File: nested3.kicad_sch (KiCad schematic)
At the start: 5 parts, among them U5 INA219AIDR

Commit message: made changes to USB circuit
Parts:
- C7: value CL05B104KO5NNNC -> 100n
- R5: value RL1206FR-070R05L -> 0.05
- R6, R7: value 1206W4F1002T5E -> 10k
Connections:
- net Battery: now reaches R5.1, U5.8 (VIN+)
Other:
- note added: "Vreg cct"
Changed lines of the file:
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@@
 		(comment 4 "Phila Haanyama, Hannah Owen")
 	)
+	(text "Vreg cct"
+		(exclude_from_sim no)
+		(at 104.648 120.142 0)
+		(effects
+			(font
+				(size 1.27 1.27)
+			)
+		)
+	)
+	(junction
+		(at 106.68 114.3)
+		(diameter 0)
+		(color 0 0 0 0)
+	)
+	(junction
+		(at 72.39 101.6)
+		(diameter 0)
+		(color 0 0 0 0)
+	)
 	(wire
 		(pts
@@
 	(wire
 		(pts
+			(xy 62.23 101.6) (xy 72.39 101.6)
+		)
+		(stroke
+			(width 0)
+			(type default)
+		)
+	)
+	(wire
+		(pts
 			(xy 104.14 88.9) (xy 107.95 88.9)
 		)
@@
 		(pts
 			(xy 143.51 114.3) (xy 147.32 114.3)
+		)
+		(stroke
+			(width 0)
+			(type default)
+		)
+	)
+	(wire
+		(pts
+			(xy 106.68 114.3) (xy 106.68 121.92)
 		)
 		(stroke
@@
 				)
 				(justify left)
+				(hide yes)
+			)
+		)
+	)
+	(global_label "Battery"
+		(shape input)
+		(at 62.23 101.6 180)
+		(fields_autoplaced yes)
+		(effects
+			(font
+				(size 1.27 1.27)
+			)
+			(justify right)
+		)
+		(property "Intersheetrefs" "${INTERSHEET_REFS}"
+			(at 52.532 101.6 0)
+			(effects
+				(font
+					(size 1.27 1.27)
+				)
+				(justify right)
 				(hide yes)
 			)
@@
 			)
 		)
-		(property "Value" "1206W4F1002T5E"
+		(property "Value" "10k"
 			(at 49.53 92.71 0)
 			(effects
@@
 			)
 		)
-		(property "Value" "RL1206FR-070R05L"
+		(property "Value" "0.05"
 			(at 85.09 110.49 0)
 			(effects
@@
 			)
 		)
-		(property "Value" "CL05B104KO5NNNC"
+		(property "Value" "100n"
 			(at 166.37 86.3599 90)
 			(effects
@@
 			)
 		)
-		(property "Value" "1206W4F1002T5E"
+		(property "Value" "10k"
 			(at 74.93 142.24 0)
 			(effects

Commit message: footprints added and usb cct finished
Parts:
- C7: footprint CL05B104KO5NNNC:CAPC1005X55N -> Capacitor_SMD:C_0402_1005Metric_Pad0.74x0.62mm_HandSolder
- R5: footprint RL1206FR-070R05L:RESC3116X65N -> Resistor_SMD:R_1206_3216Metric_Pad1.30x1.75mm_HandSolder
- R6, R7: footprint 1206W4F1002T5E:RESC3115X65N -> Resistor_SMD:R_1206_3216Metric_Pad1.30x1.75mm_HandSolder
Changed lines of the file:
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@@
 			)
 		)
-		(property "Footprint" "1206W4F1002T5E:RESC3115X65N"
+		(property "Footprint" "Resistor_SMD:R_1206_3216Metric_Pad1.30x1.75mm_HandSolder"
 			(at 49.53 96.52 0)
 			(effects
@@
 			)
 		)
-		(property "Footprint" "RL1206FR-070R05L:RESC3116X65N"
+		(property "Footprint" "Resistor_SMD:R_1206_3216Metric_Pad1.30x1.75mm_HandSolder"
 			(at 85.09 114.3 0)
 			(effects
@@
 			)
 		)
-		(property "Footprint" "CL05B104KO5NNNC:CAPC1005X55N"
+		(property "Footprint" "Capacitor_SMD:C_0402_1005Metric_Pad0.74x0.62mm_HandSolder"
 			(at 162.56 83.82 0)
 			(effects
@@
 			)
 		)
-		(property "Footprint" "1206W4F1002T5E:RESC3115X65N"
+		(property "Footprint" "Resistor_SMD:R_1206_3216Metric_Pad1.30x1.75mm_HandSolder"
 			(at 74.93 146.05 0)
 			(effects

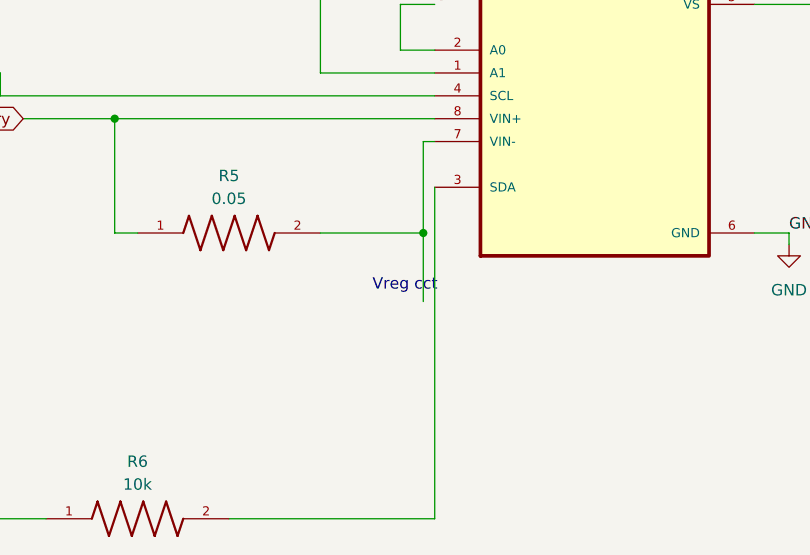
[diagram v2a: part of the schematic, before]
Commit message: added LCSC numbers and finsihed footprints
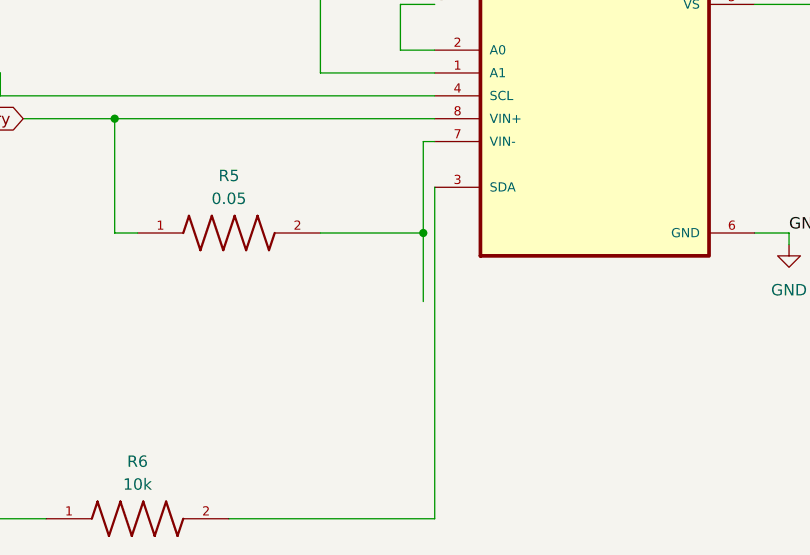
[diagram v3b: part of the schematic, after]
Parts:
- C7: LCSC (none) -> C1525
- R5: LCSC (none) -> C375525
- R6, R7: LCSC (none) -> C17902
- U5: footprint INA219AIDR:SOIC127P599X175-8N -> Package_SO:SOIC-8_3.9x4.9mm_P1.27mm; LCSC (none) -> C138706
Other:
- note removed: "Vreg cct"
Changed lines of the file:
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@@
 		(comment 4 "Phila Haanyama, Hannah Owen")
-	)
-	(text "Vreg cct"
-		(exclude_from_sim no)
-		(at 104.648 120.142 0)
-		(effects
-			(font
-				(size 1.27 1.27)
-			)
-		)
 	)
 	(junction
@@
 			)
 		)
+		(property "LCSC" "C17902"
+			(at 49.53 96.52 0)
+			(effects
+				(font
+					(size 1.27 1.27)
+				)
+				(hide yes)
+			)
+		)
 		(pin "1"
 		)
@@
 			)
 		)
+		(property "LCSC" "C375525"
+			(at 85.09 114.3 0)
+			(effects
+				(font
+					(size 1.27 1.27)
+				)
+				(hide yes)
+			)
+		)
 		(pin "2"
 		)
@@
 			)
 		)
+		(property "LCSC" "C1525"
+			(at 162.56 83.82 90)
+			(effects
+				(font
+					(size 1.27 1.27)
+				)
+				(hide yes)
+			)
+		)
 		(pin "1"
 		)
@@
 			)
 		)
-		(property "Footprint" "INA219AIDR:SOIC127P599X175-8N"
+		(property "Footprint" "Package_SO:SOIC-8_3.9x4.9mm_P1.27mm"
 			(at 125.73 101.6 0)
 			(effects
@@
 				)
 				(justify bottom)
+				(hide yes)
+			)
+		)
+		(property "LCSC" "C138706"
+			(at 125.73 101.6 0)
+			(effects
+				(font
+					(size 1.27 1.27)
+				)
 				(hide yes)
 			)
@@
 				(hide yes)
 			)
+		)
+		(property "LCSC" "C17902"
+			(at 74.93 146.05 0)
+			(effects
+				(font
+					(size 1.27 1.27)
+				)
+				(hide yes)
+			)

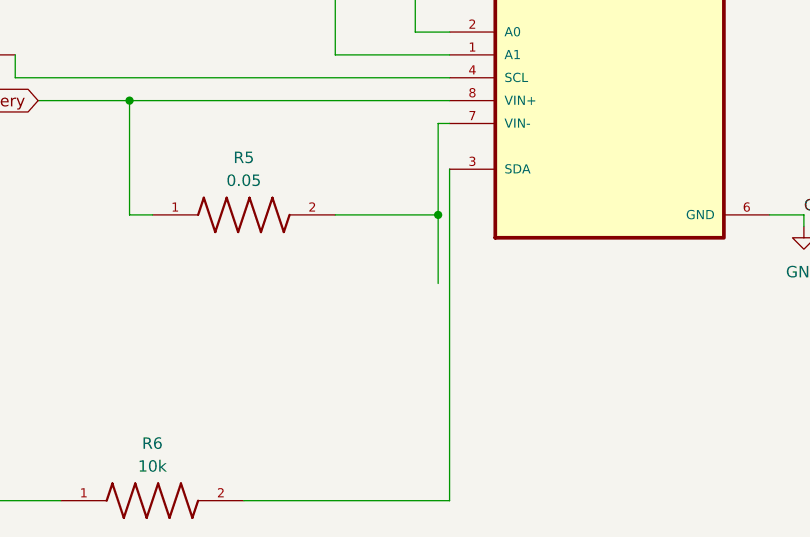
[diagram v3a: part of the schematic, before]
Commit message: Removed old backups and updated KiCad files
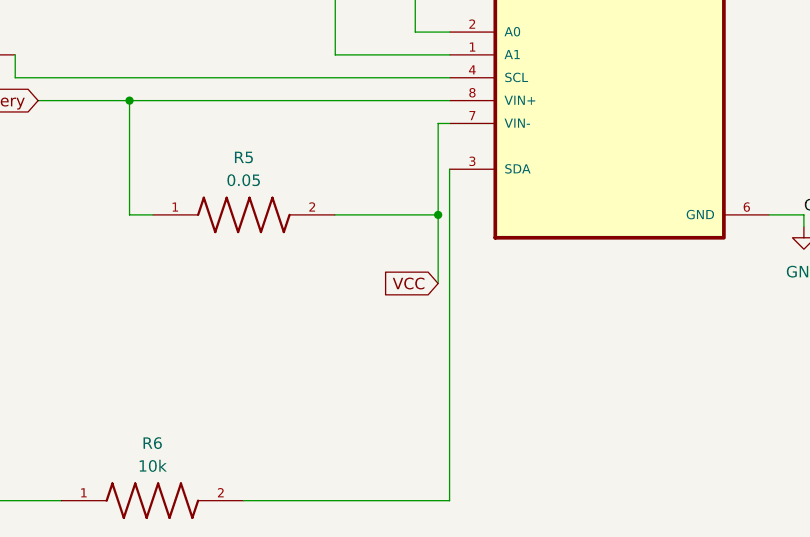
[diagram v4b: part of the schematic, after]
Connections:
- net VCC: now reaches R5.2, U5.7 (VIN-)
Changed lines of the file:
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@@
+		)
+	)
+	(global_label "VCC"
+		(shape input)
+		(at 106.68 121.92 180)
+		(fields_autoplaced yes)
+		(effects
+			(font
+				(size 1.27 1.27)
+			)
+			(justify right)
+		)
+		(property "Intersheetrefs" "${INTERSHEET_REFS}"
+			(at 100.0662 121.92 0)
+			(effects
+				(font
+					(size 1.27 1.27)
+				)
+				(justify right)
+				(hide yes)
+			)
 		)
 	)

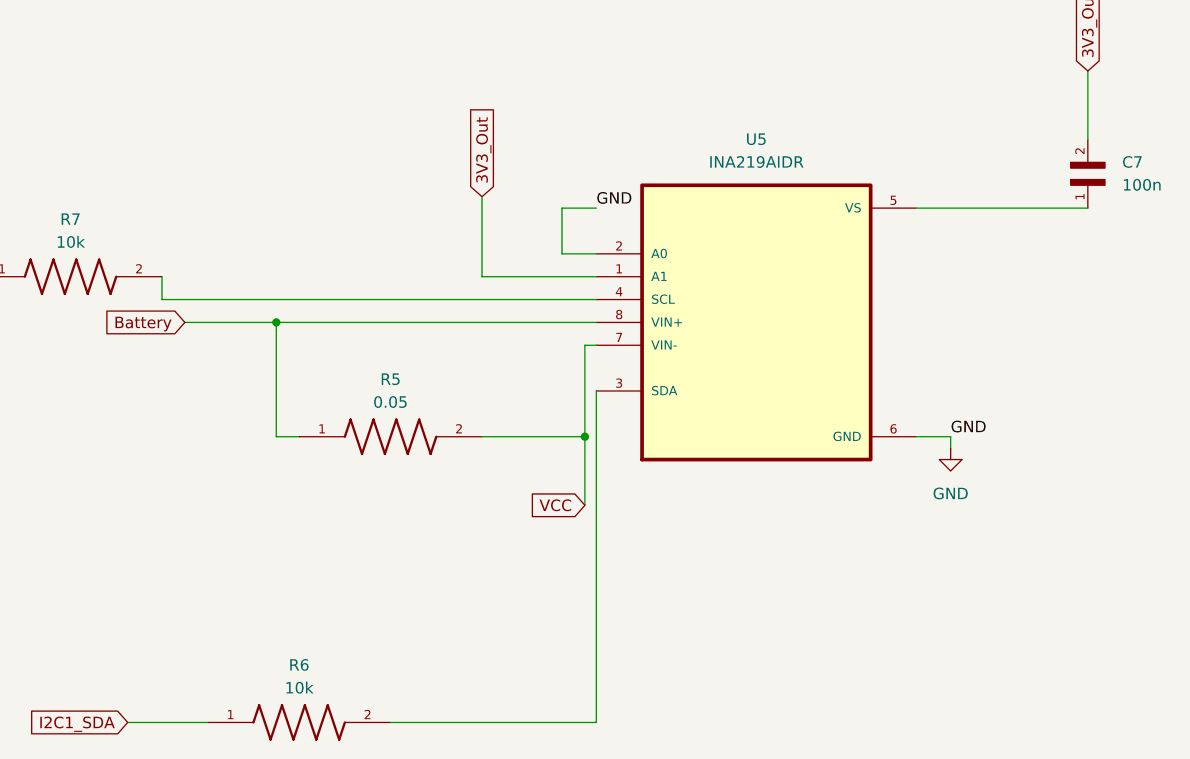
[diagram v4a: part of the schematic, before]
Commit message: Removed old backups and updated KiCad files
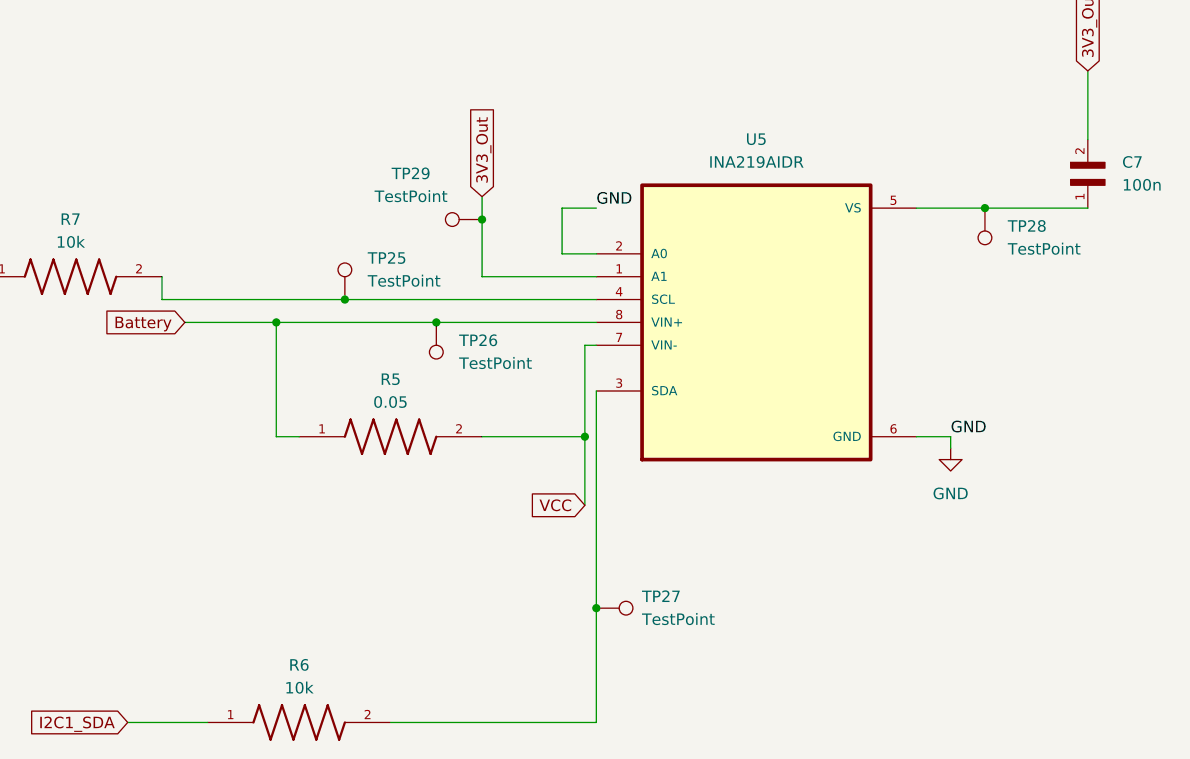
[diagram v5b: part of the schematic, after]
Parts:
- added TP25, TP26, TP27, TP28, TP29: TestPoint, TestPoint:TestPoint_Pad_1.0x1.0mm, symbol Connector:TestPoint
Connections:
- net 3V3_Out: now also TP29.1
- net Battery: now also TP26.1
- net at R7.2, U5.4 (SCL): now also TP25.1
- net at C7.1, U5.5 (VS): now also TP28.1
- net at R6.2, U5.3 (SDA): now also TP27.1

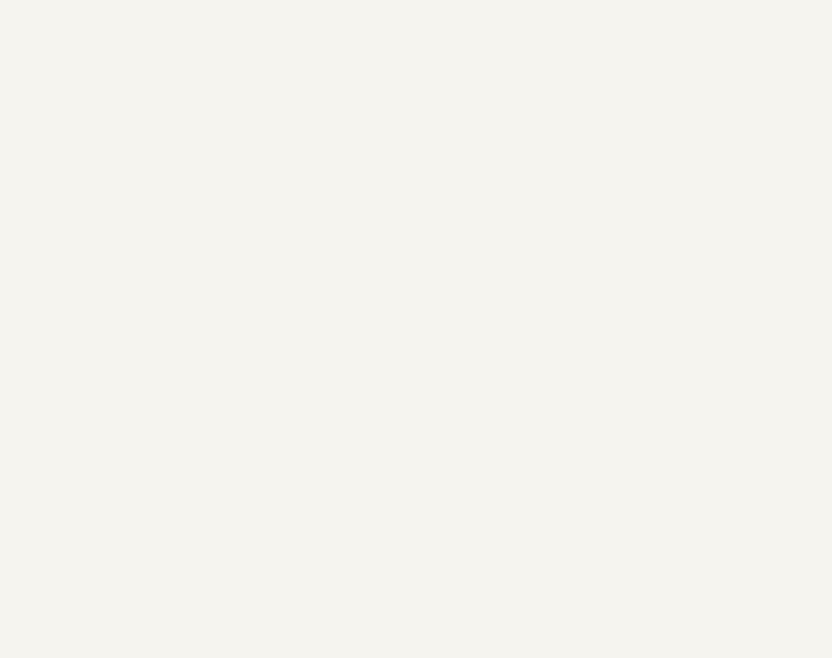
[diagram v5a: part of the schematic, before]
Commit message: Removed old backups and updated KiCad files
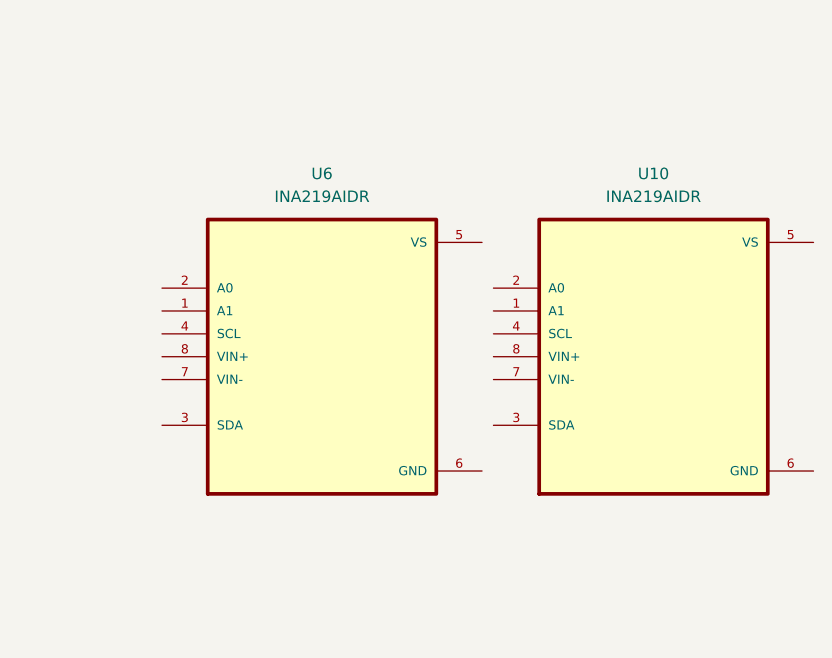
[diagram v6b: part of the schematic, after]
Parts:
- added U10, U6: INA219AIDR, Package_SO:SOIC-8_3.9x4.9mm_P1.27mm, symbol INA219AIDR[1]:INA219AIDR

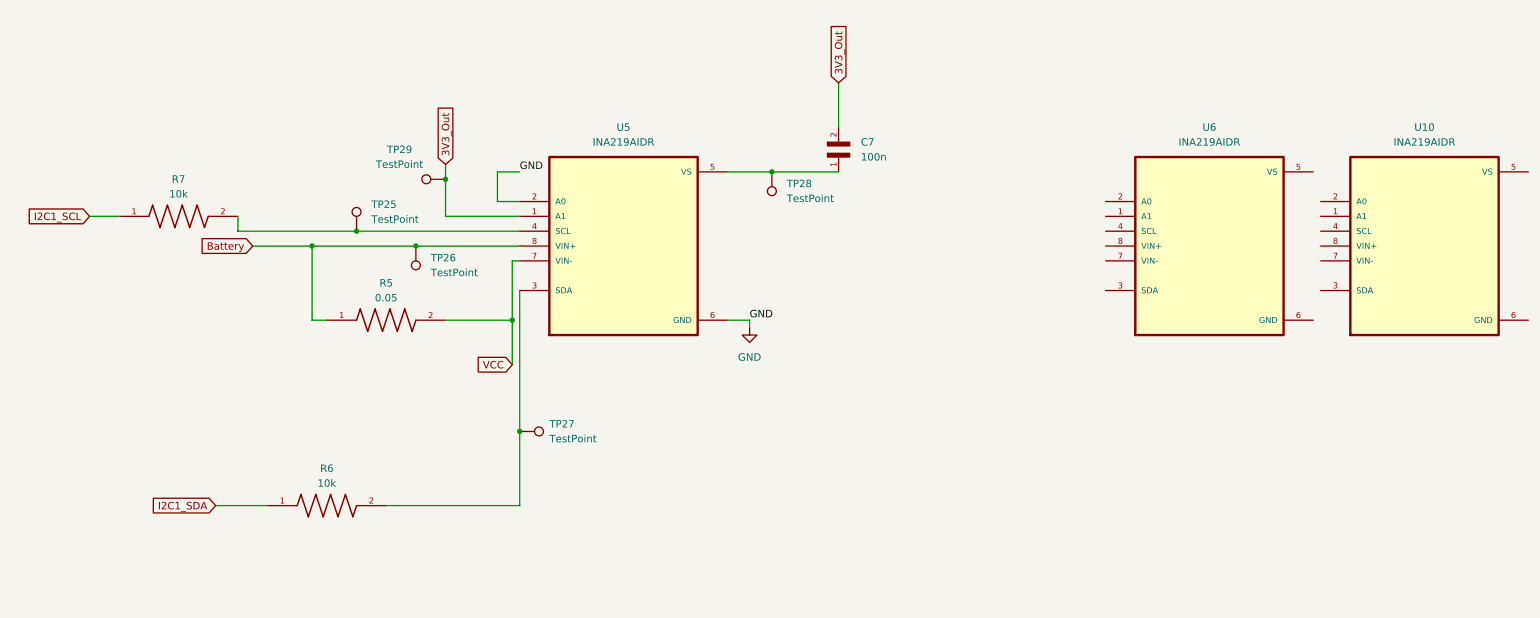
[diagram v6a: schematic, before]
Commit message: Removed old backups and updated KiCad files
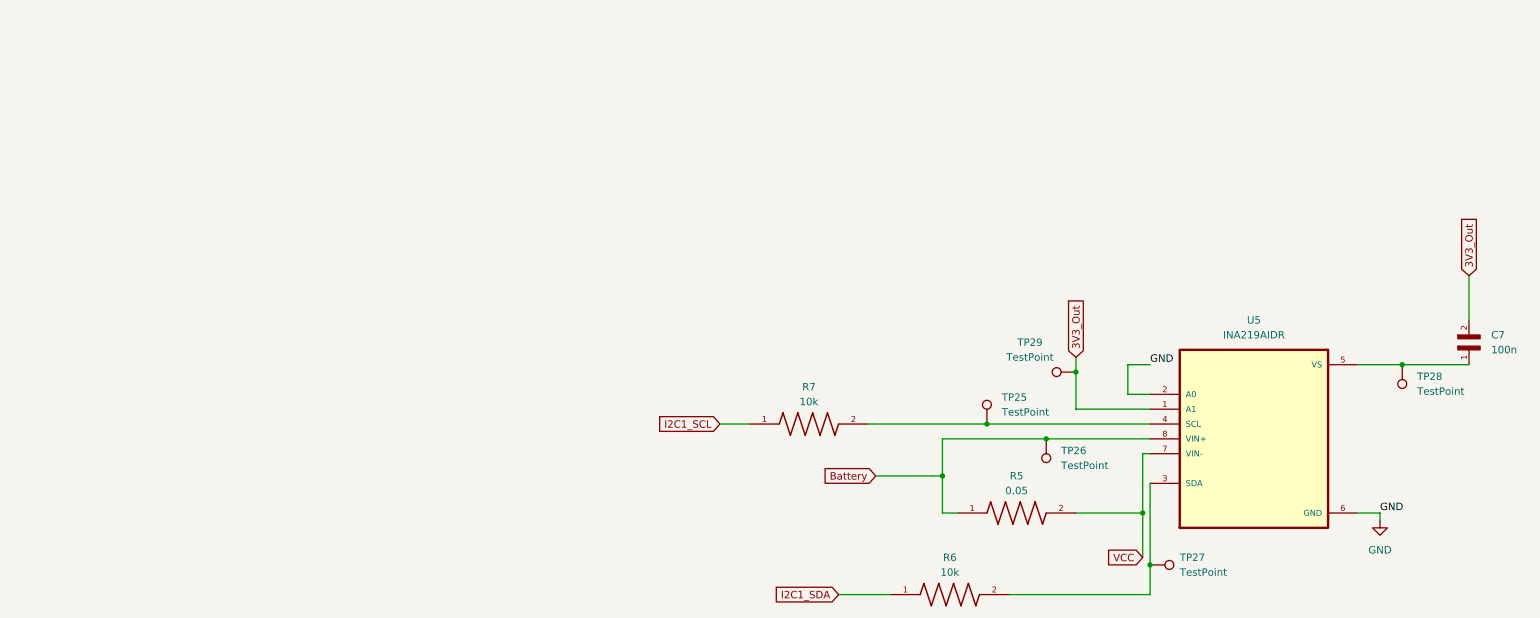
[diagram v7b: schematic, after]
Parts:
- removed U10, U6: INA219AIDR, Package_SO:SOIC-8_3.9x4.9mm_P1.27mm, symbol INA219AIDR[1]:INA219AIDR
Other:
- title: (none) -> MICRO-MOUSE POWER SUBSYSTEM
- moved on the sheet: C7, R5, R6, R7, TP25, TP26, TP27, TP28, TP29, U5
